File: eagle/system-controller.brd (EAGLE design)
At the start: 99 x 100 mm, 226 parts, among them J1 1, Q1 MOSFET-P-N-PAIR, Q10 MOSFET-P-N-PAIR, Q11 DNP/NTR4101P, Q2 MOSFET-P-N-PAIR, Q3 DON3035L, Q4 MOSFET-P-N-PAIR, Q5 MOSFET-P-N-PAIR, Q6 MOSFET-P-N-PAIR, Q7 MOSFET-P-N-PAIR, Q8 MOSFET-P-N-PAIR, Q9 DNP/NTR4101P, U1 TPS25944LRVCRWQFN-20-3X4, U10 TPS25944LRVCRWQFN-20-3X4, U11 ACPL-M61L, U12 ACPL-M61L, U13 TPS25944LRVCRWQFN-20-3X4, U14 ACPL-M61L, U15 ACPL-M61L, U2 LP5907MFX-3.0, U3 TPS25944LRVCRWQFN-20-3X4, U4 TPS25944LRVCRWQFN-20-3X4, U5 TPS25944LRVCRWQFN-20-3X4, U6 TPS25944LRVCRWQFN-20-3X4, U7 ATMEGA128L-8A(U/N), U8 TS4100, U9 TPS25944LRVCRWQFN-20-3X4, X1 8 MHz CRYSTAL-ABRACON-ABM3-SMD

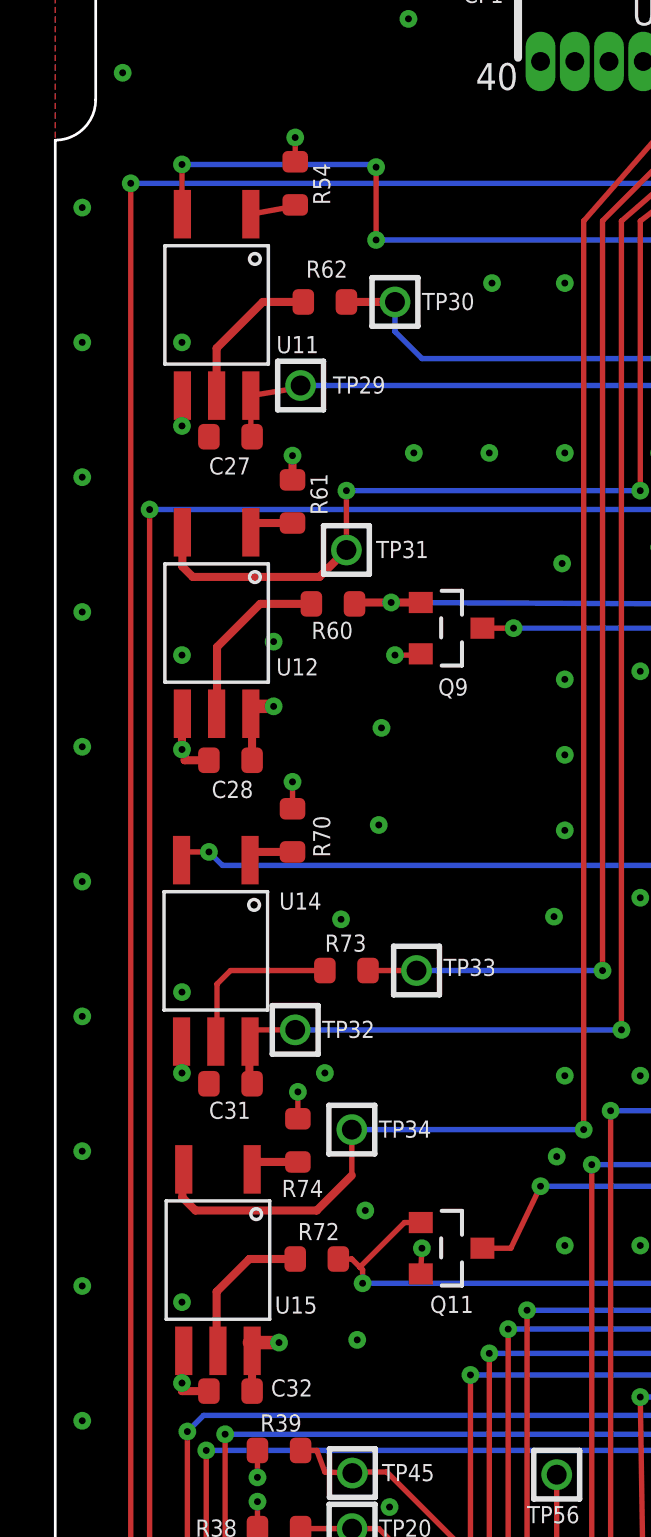
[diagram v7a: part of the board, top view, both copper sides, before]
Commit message: Fixed opto-isolator symbol with proper labels
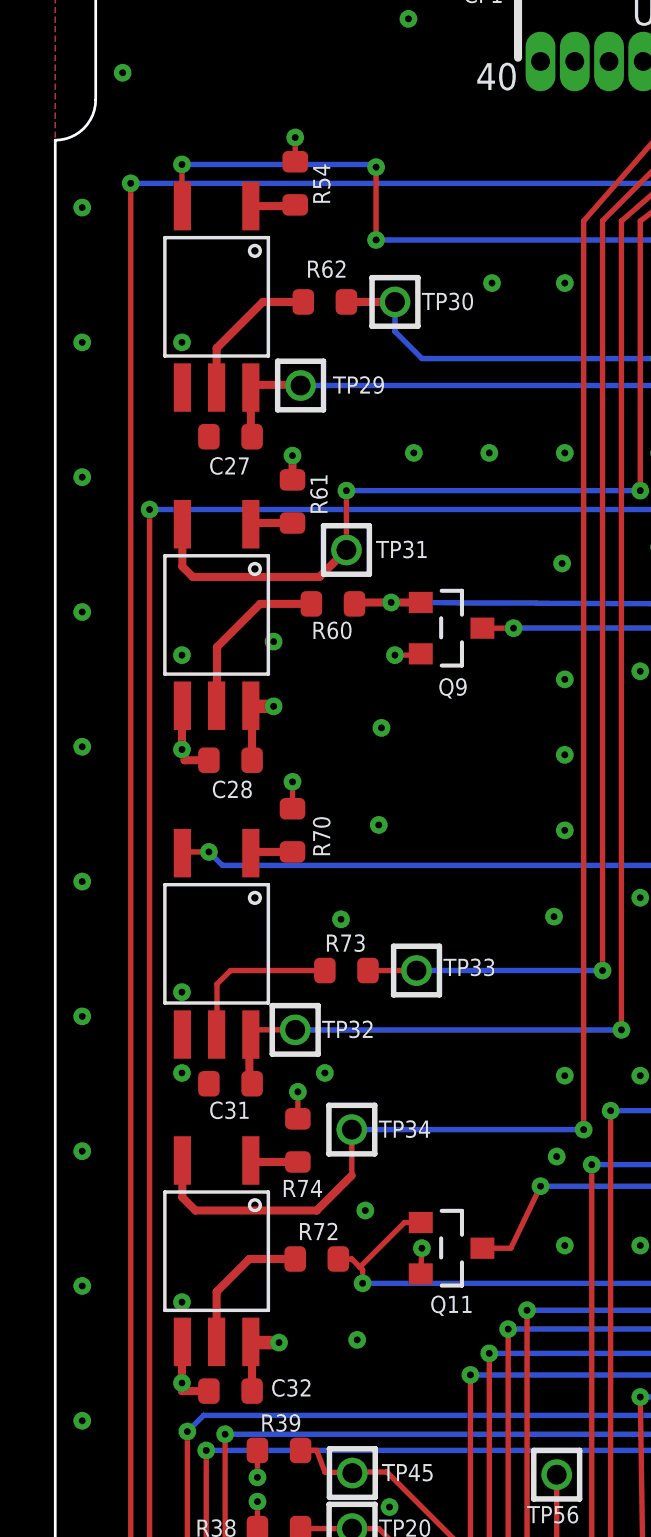
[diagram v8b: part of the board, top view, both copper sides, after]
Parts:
- removed U11, U12, U14, U15: ACPL-M61L, v2_sync_box:ACPL-M61L
- added U$1, U$2, U$3, U$4: ACPL-M61L, system-controller:ACPL-M61L
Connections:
- net 3V: now also U$3.5, U$4.5; no longer U12.5, U15.5
- net GND: now also U$1.3, U$2.3, U$3.3, U$4.3; no longer U11.3, U12.3, U14.3, U15.3
- net N$16: now also U$2.4; no longer U14.4
- net N$18: now also U$4.4; no longer U15.4
- net N$24: now also U$3.4; no longer U12.4
- net N$4: now also U$2.1; no longer U14.1
- net N$5: now also U$1.4; no longer U11.4
- net N$54: now also U$4.1; no longer U15.1
- net N$58: now also U$1.1; no longer U11.1
- net N$8: now also U$3.1; no longer U12.1
- net TXD0: now also U$2.2; no longer U14.2
- net TXD1: now also U$1.2; no longer U11.2
- net UART_FC_TX: now also U$3.2; no longer U12.2
- net UART_FC_VCC: now also U$1.5; no longer U11.5
- net UART_LGR_TX: now also U$4.2; no longer U15.2
- net UART_LGR_VCC: now also U$2.5; no longer U14.5
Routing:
- net GND: track 33.3 -> 31.0 mm, vias 357 -> 356
- net N$16: track 6.65 -> 6.10 mm
